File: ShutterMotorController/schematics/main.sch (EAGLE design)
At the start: 51 parts, among them IC1 MC34063AD, IC2 ULN2003AD, IC3 78L05SMD, J1 SCREW-TERMINAL-2PIN, J2 SCREW-TERMINAL-2PIN, J3 SCREW-TERMINAL-2PIN, J4 SCREW-TERMINAL-2PIN, J5 PWR_IN, K1 35701331, K2 35701331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

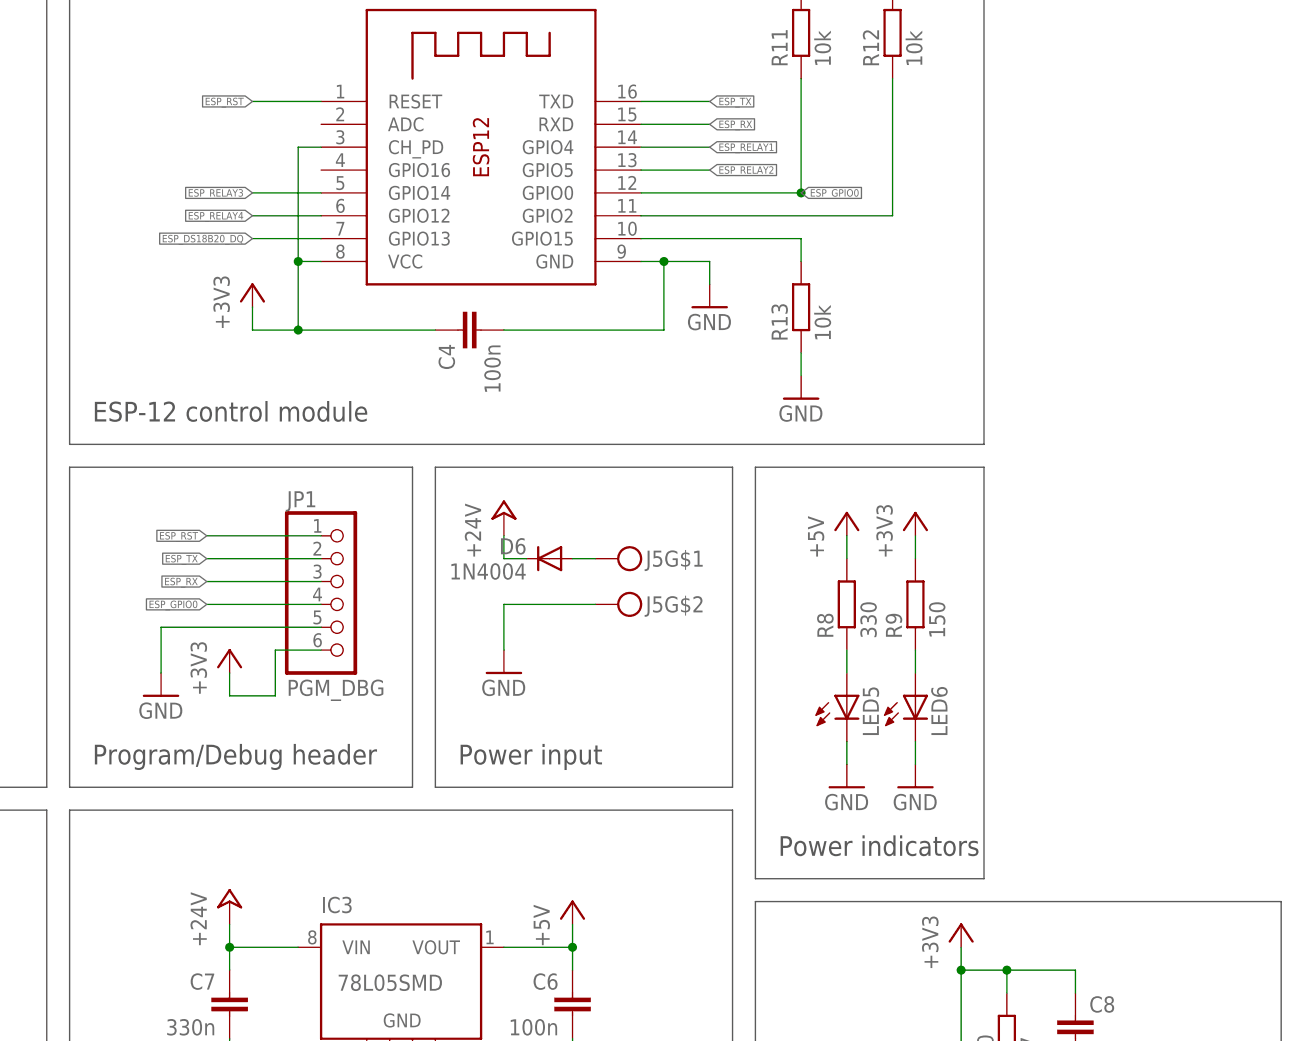
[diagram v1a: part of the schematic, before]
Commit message: SMC: add indicator LED
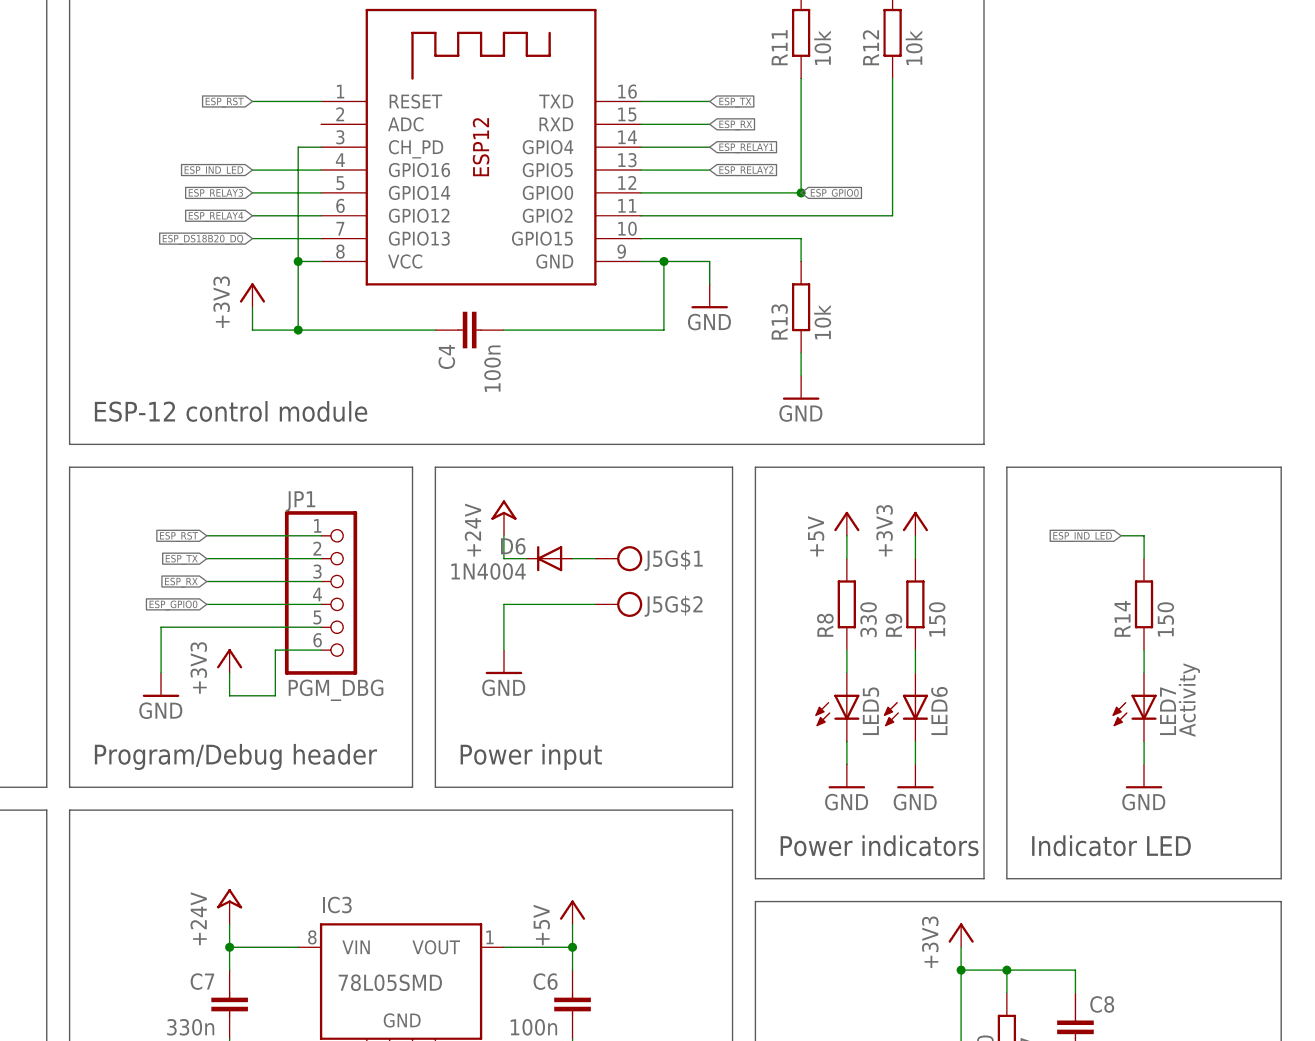
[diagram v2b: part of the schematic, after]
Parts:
- added LED7: Activity, led:LED5MM
- added R14: 150, rcl:R-EU_R1206
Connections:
- new net ESP_IND_LED: R14.2, X1.GPIO16
- new net N$27: LED7.A, R14.1
- net GND: now also LED7.C
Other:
- note added: "Indicator LED"
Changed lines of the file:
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@@
 <?xml version="1.0" encoding="utf-8"?>
 <!DOCTYPE eagle SYSTEM "eagle.dtd">
-<eagle version="8.5.1">
+<eagle version="8.6.1">
 <drawing>
 <settings>
@@
 <part name="R12" library="rcl" library_urn="urn:adsk.eagle:library:334" deviceset="R-EU_" device="R1206" package3d_urn="urn:adsk.eagle:package:23540/2" value="10k"/>
 <part name="C9" library="rcl" library_urn="urn:adsk.eagle:library:334" deviceset="C-EU" device="C1206" package3d_urn="urn:adsk.eagle:package:23618/2" value="100n"/>
+<part name="LED7" library="led" library_urn="urn:adsk.eagle:library:259" deviceset="LED" device="5MM" package3d_urn="urn:adsk.eagle:package:15799/2" value="Activity"/>
+<part name="R14" library="rcl" library_urn="urn:adsk.eagle:library:334" deviceset="R-EU_" device="R1206" package3d_urn="urn:adsk.eagle:package:23540/2" value="150"/>
+<part name="GND17" library="supply1" library_urn="urn:adsk.eagle:library:371" deviceset="GND" device=""/>
 </parts>
 <sheets>
@@
 <wire x1="264.16" y1="2.54" x2="205.74" y2="2.54" width="0.1524" layer="97"/>
 <text x="208.28" y="5.08" size="2.1844" layer="97">DS18B20 temperature sensor</text>
+<wire x1="233.68" y1="91.44" x2="233.68" y2="45.72" width="0.1524" layer="97"/>
+<wire x1="233.68" y1="45.72" x2="264.16" y2="45.72" width="0.1524" layer="97"/>
+<wire x1="264.16" y1="45.72" x2="264.16" y2="91.44" width="0.1524" layer="97"/>
+<wire x1="264.16" y1="91.44" x2="233.68" y2="91.44" width="0.1524" layer="97"/>
+<text x="236.22" y="48.26" size="2.1844" layer="97">Indicator LED</text>
 </plain>
 <instances>
@@
 <instance part="R12" gate="G$1" x="220.98" y="139.7" rot="R90"/>
 <instance part="C9" gate="G$1" x="27.94" y="86.36" rot="MR270"/>
+<instance part="LED7" gate="G$1" x="248.92" y="66.04"/>
+<instance part="R14" gate="G$1" x="248.92" y="76.2" rot="R90"/>
+<instance part="GND17" gate="1" x="248.92" y="55.88"/>
 </instances>
 <busses>
@@
 <pinref part="GND16" gate="1" pin="GND"/>
 <wire x1="210.82" y1="104.14" x2="210.82" y2="101.6" width="0.1524" layer="91"/>
+</segment>
+<segment>
+<pinref part="LED7" gate="G$1" pin="C"/>
+<pinref part="GND17" gate="1" pin="GND"/>
+<wire x1="248.92" y1="60.96" x2="248.92" y2="58.42" width="0.1524" layer="91"/>
 </segment>
 </net>
@@
 </segment>
 </net>
+<net name="N$27" class="0">
+<segment>
+<pinref part="R14" gate="G$1" pin="1"/>
+<pinref part="LED7" gate="G$1" pin="A"/>
+<wire x1="248.92" y1="71.12" x2="248.92" y2="68.58" width="0.1524" layer="91"/>
+</segment>
+</net>
+<net name="ESP_IND_LED" class="0">
+<segment>
+<pinref part="R14" gate="G$1" pin="2"/>
+<wire x1="248.92" y1="81.28" x2="248.92" y2="83.82" width="0.1524" layer="91"/>
+<wire x1="248.92" y1="83.82" x2="246.38" y2="83.82" width="0.1524" layer="91"/>
+<label x="246.38" y="83.82" size="0.8128" layer="95" rot="R180" xref="yes"/>
+</segment>
+<segment>
+<pinref part="X1" gate="G$1" pin="GPIO16"/>
+<wire x1="157.48" y1="124.46" x2="149.86" y2="124.46" width="0.1524" layer="91"/>
+<label x="149.86" y="124.46" size="0.8128" layer="95" rot="R180" xref="yes"/>
+</segment>
+</net>

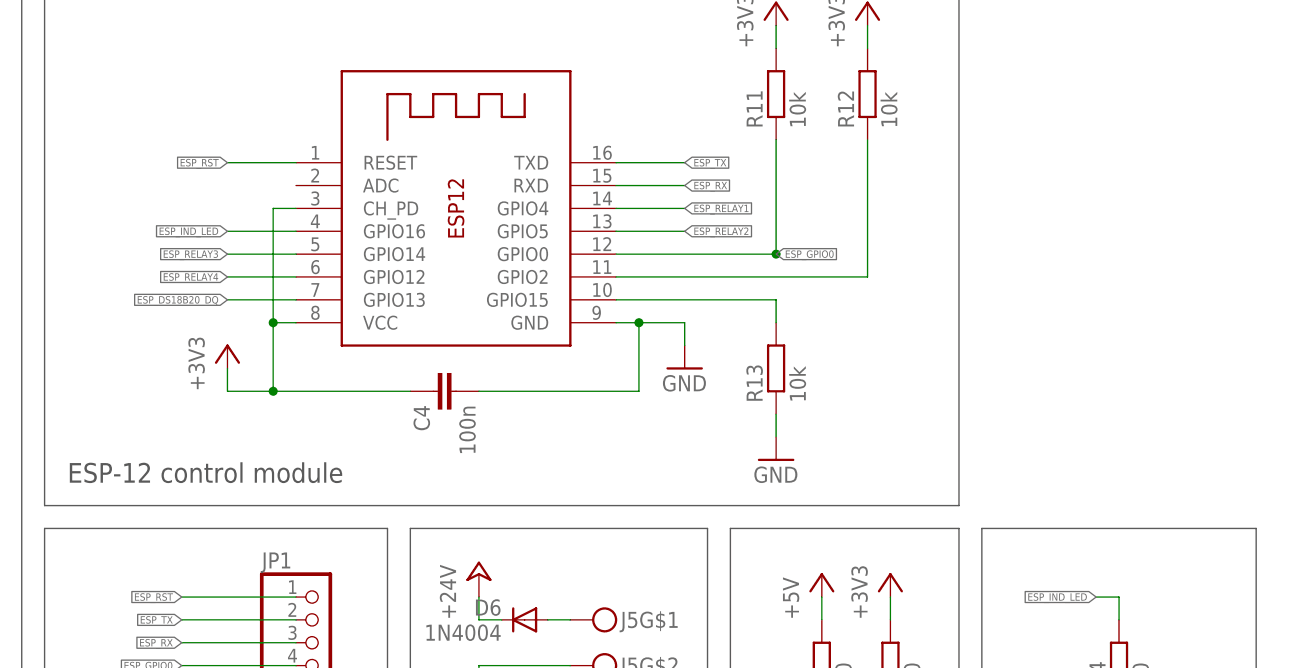
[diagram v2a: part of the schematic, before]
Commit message: SMC: add ADC header to the PCB
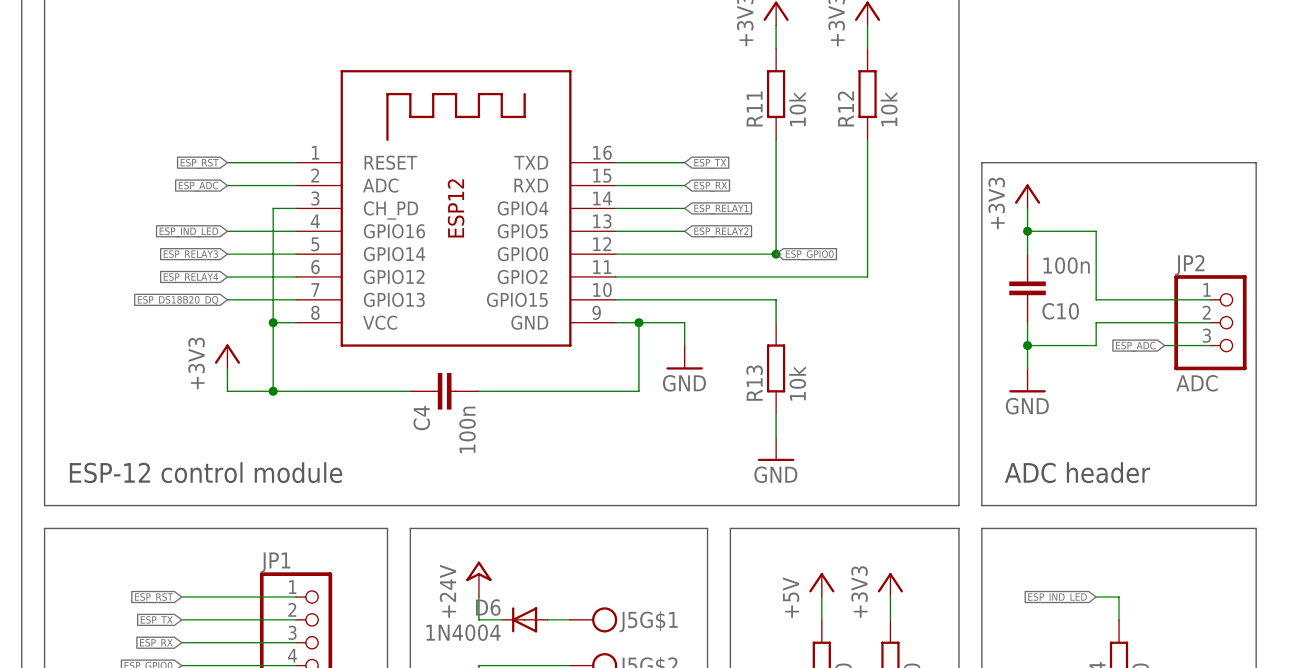
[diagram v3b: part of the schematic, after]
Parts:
- added C10: 100n, rcl:C-EUC1206
- added JP2: ADC, pinhead:PINHD-1X3
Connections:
- new net ESP_ADC: JP2.3, X1.ADC
- net +3V3: now also C10.2, JP2.1
- net GND: now also C10.1, JP2.2
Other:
- note added: "ADC header"
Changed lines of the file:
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@@
 <part name="R14" library="rcl" library_urn="urn:adsk.eagle:library:334" deviceset="R-EU_" device="R1206" package3d_urn="urn:adsk.eagle:package:23540/2" value="150"/>
 <part name="GND17" library="supply1" library_urn="urn:adsk.eagle:library:371" deviceset="GND" device=""/>
+<part name="JP2" library="pinhead" library_urn="urn:adsk.eagle:library:325" deviceset="PINHD-1X3" device="" package3d_urn="urn:adsk.eagle:package:22458/2" value="ADC"/>
+<part name="+3V8" library="supply1" library_urn="urn:adsk.eagle:library:371" deviceset="+3V3" device=""/>
+<part name="GND18" library="supply1" library_urn="urn:adsk.eagle:library:371" deviceset="GND" device=""/>
+<part name="C10" library="rcl" library_urn="urn:adsk.eagle:library:334" deviceset="C-EU" device="C1206" package3d_urn="urn:adsk.eagle:package:23618/2" value="100n"/>
 </parts>
 <sheets>
@@
 <wire x1="264.16" y1="91.44" x2="233.68" y2="91.44" width="0.1524" layer="97"/>
 <text x="236.22" y="48.26" size="2.1844" layer="97">Indicator LED</text>
+<wire x1="233.68" y1="93.98" x2="264.16" y2="93.98" width="0.1524" layer="97"/>
+<wire x1="264.16" y1="93.98" x2="264.16" y2="132.08" width="0.1524" layer="97"/>
+<wire x1="264.16" y1="132.08" x2="233.68" y2="132.08" width="0.1524" layer="97"/>
+<wire x1="233.68" y1="132.08" x2="233.68" y2="93.98" width="0.1524" layer="97"/>
+<text x="236.22" y="96.52" size="2.1844" layer="97">ADC header</text>
 </plain>
 <instances>
@@
 <instance part="R14" gate="G$1" x="248.92" y="76.2" rot="R90"/>
 <instance part="GND17" gate="1" x="248.92" y="55.88"/>
+<instance part="JP2" gate="A" x="261.62" y="114.3"/>
+<instance part="+3V8" gate="G$1" x="238.76" y="129.54"/>
+<instance part="GND18" gate="1" x="238.76" y="106.68"/>
+<instance part="C10" gate="G$1" x="238.76" y="116.84" rot="MR180"/>
 </instances>
 <busses>
@@
 <wire x1="248.92" y1="60.96" x2="248.92" y2="58.42" width="0.1524" layer="91"/>
 </segment>
+<segment>
+<pinref part="C10" gate="G$1" pin="1"/>
+<pinref part="GND18" gate="1" pin="GND"/>
+<wire x1="238.76" y1="109.22" x2="238.76" y2="111.76" width="0.1524" layer="91"/>
+<pinref part="JP2" gate="A" pin="2"/>
+<wire x1="238.76" y1="111.76" x2="238.76" y2="114.3" width="0.1524" layer="91"/>
+<wire x1="259.08" y1="114.3" x2="246.38" y2="114.3" width="0.1524" layer="91"/>
+<wire x1="246.38" y1="114.3" x2="246.38" y2="111.76" width="0.1524" layer="91"/>
+<wire x1="246.38" y1="111.76" x2="238.76" y2="111.76" width="0.1524" layer="91"/>
+<junction x="238.76" y="111.76"/>
+</segment>
 </net>
 <net name="N$5" class="0">
@@
 <wire x1="220.98" y1="144.78" x2="220.98" y2="147.32" width="0.1524" layer="91"/>
 <pinref part="R12" gate="G$1" pin="2"/>
+</segment>
+<segment>
+<pinref part="C10" gate="G$1" pin="2"/>
+<pinref part="+3V8" gate="G$1" pin="+3V3"/>
+<wire x1="238.76" y1="121.92" x2="238.76" y2="124.46" width="0.1524" layer="91"/>
+<pinref part="JP2" gate="A" pin="1"/>
+<wire x1="238.76" y1="124.46" x2="238.76" y2="127" width="0.1524" layer="91"/>
+<wire x1="259.08" y1="116.84" x2="246.38" y2="116.84" width="0.1524" layer="91"/>
+<wire x1="246.38" y1="116.84" x2="246.38" y2="124.46" width="0.1524" layer="91"/>
+<wire x1="246.38" y1="124.46" x2="238.76" y2="124.46" width="0.1524" layer="91"/>
+<junction x="238.76" y="124.46"/>
 </segment>
 </net>
@@
 </segment>
 </net>
+<net name="ESP_ADC" class="0">
+<segment>
+<pinref part="X1" gate="G$1" pin="ADC"/>
+<wire x1="157.48" y1="129.54" x2="149.86" y2="129.54" width="0.1524" layer="91"/>
+<label x="149.86" y="129.54" size="0.8128" layer="95" rot="R180" xref="yes"/>
+</segment>
+<segment>
+<pinref part="JP2" gate="A" pin="3"/>
+<wire x1="259.08" y1="111.76" x2="254" y2="111.76" width="0.1524" layer="91"/>
+<label x="254" y="111.76" size="0.8128" layer="95" rot="R180" xref="yes"/>
+</segment>
+</net>

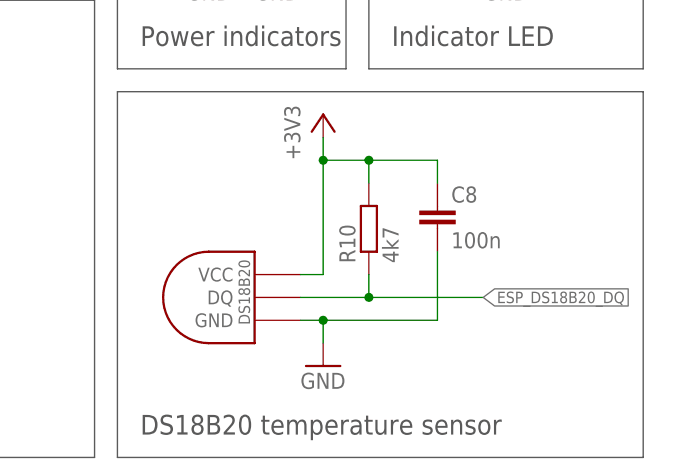
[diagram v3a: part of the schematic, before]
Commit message: SMC: fix DRC errors of board design
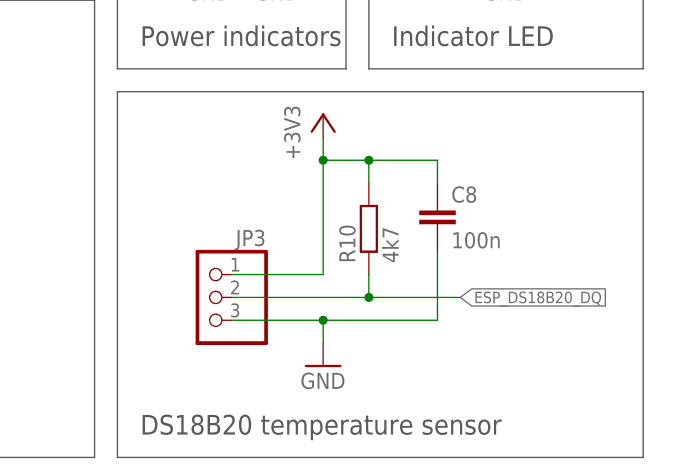
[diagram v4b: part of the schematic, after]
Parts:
- removed U$1: DS1820TO92, Ava:DS1820TO92
- added JP3: (no value), pinhead:PINHD-1X3
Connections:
- net +3V3: now also JP3.1; no longer U$1.VCC
- net ESP_DS18B20_DQ: now also JP3.2; no longer U$1.DQ
- net GND: now also JP3.3; no longer U$1.GND
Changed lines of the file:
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@@
 <part name="LED6" library="led" library_urn="urn:adsk.eagle:library:259" deviceset="LED" device="5MM" package3d_urn="urn:adsk.eagle:package:15799/2"/>
 <part name="+3V4" library="supply1" library_urn="urn:adsk.eagle:library:371" deviceset="+3V3" device=""/>
-<part name="U$1" library="Ava" deviceset="DS1820" device="TO92"/>
 <part name="R10" library="rcl" library_urn="urn:adsk.eagle:library:334" deviceset="R-EU_" device="R1206" package3d_urn="urn:adsk.eagle:package:23540/2" value="4k7"/>
 <part name="+3V5" library="supply1" library_urn="urn:adsk.eagle:library:371" deviceset="+3V3" device=""/>
@@
 <part name="GND18" library="supply1" library_urn="urn:adsk.eagle:library:371" deviceset="GND" device=""/>
 <part name="C10" library="rcl" library_urn="urn:adsk.eagle:library:334" deviceset="C-EU" device="C1206" package3d_urn="urn:adsk.eagle:package:23618/2" value="100n"/>
+<part name="JP3" library="pinhead" library_urn="urn:adsk.eagle:library:325" deviceset="PINHD-1X3" device="" package3d_urn="urn:adsk.eagle:package:22458/2"/>
 </parts>
 <sheets>
@@
 <instance part="LED6" gate="G$1" x="223.52" y="66.04"/>
 <instance part="+3V4" gate="G$1" x="147.32" y="71.12"/>
-<instance part="U$1" gate="G$1" x="220.98" y="20.32" rot="R90"/>
 <instance part="R10" gate="G$1" x="233.68" y="27.94" rot="R90"/>
 <instance part="+3V5" gate="G$1" x="228.6" y="40.64"/>
@@
 <instance part="GND18" gate="1" x="238.76" y="106.68"/>
 <instance part="C10" gate="G$1" x="238.76" y="116.84" rot="MR180"/>
+<instance part="JP3" gate="A" x="215.9" y="20.32" rot="MR0"/>
 </instances>
 <busses>
@@
 </segment>
 <segment>
-<pinref part="U$1" gate="G$1" pin="GND"/>
-<wire x1="226.06" y1="17.78" x2="228.6" y2="17.78" width="0.1524" layer="91"/>
 <pinref part="GND15" gate="1" pin="GND"/>
 <wire x1="228.6" y1="17.78" x2="228.6" y2="15.24" width="0.1524" layer="91"/>
@@
 <wire x1="241.3" y1="17.78" x2="241.3" y2="25.4" width="0.1524" layer="91"/>
 <junction x="228.6" y="17.78"/>
+<pinref part="JP3" gate="A" pin="3"/>
+<wire x1="228.6" y1="17.78" x2="218.44" y2="17.78" width="0.1524" layer="91"/>
 </segment>
 <segment>
@@
 </segment>
 <segment>
-<pinref part="U$1" gate="G$1" pin="VCC"/>
 <pinref part="+3V5" gate="G$1" pin="+3V3"/>
-<wire x1="226.06" y1="22.86" x2="228.6" y2="22.86" width="0.1524" layer="91"/>
 <wire x1="228.6" y1="22.86" x2="228.6" y2="35.56" width="0.1524" layer="91"/>
 <pinref part="R10" gate="G$1" pin="2"/>
@@
 <pinref part="C8" gate="G$1" pin="1"/>
 <wire x1="241.3" y1="35.56" x2="241.3" y2="33.02" width="0.1524" layer="91"/>
+<pinref part="JP3" gate="A" pin="1"/>
+<wire x1="228.6" y1="22.86" x2="218.44" y2="22.86" width="0.1524" layer="91"/>
 </segment>
 <segment>
@@
 <net name="ESP_DS18B20_DQ" class="0">
 <segment>
-<pinref part="U$1" gate="G$1" pin="DQ"/>
 <pinref part="R10" gate="G$1" pin="1"/>
-<wire x1="226.06" y1="20.32" x2="233.68" y2="20.32" width="0.1524" layer="91"/>
 <wire x1="233.68" y1="20.32" x2="233.68" y2="22.86" width="0.1524" layer="91"/>
-<wire x1="233.68" y1="20.32" x2="246.38" y2="20.32" width="0.1524" layer="91"/>
+<wire x1="233.68" y1="20.32" x2="243.84" y2="20.32" width="0.1524" layer="91"/>
 <junction x="233.68" y="20.32"/>
-<label x="246.38" y="20.32" size="1.27" layer="95" xref="yes"/>
-</segment>
-<segment>
+<label x="243.84" y="20.32" size="1.27" layer="95" xref="yes"/>
+<pinref part="JP3" gate="A" pin="2"/>
+<wire x1="233.68" y1="20.32" x2="218.44" y2="20.32" width="0.1524" layer="91"/>
+</segment>
+<segment>
